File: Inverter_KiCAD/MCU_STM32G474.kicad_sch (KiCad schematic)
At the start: 42 parts, among them J801 USB_C_Receptacle_USB2.0, J802 Conn_01x05, J803 Conn_ST_STDC14, J804 Conn_01x04, SW801 SW_Push, SW802 SW_Push, SW803 SW_Push, SW804 SW_Push, SW805 SW_Push, U801 STM32G474RETx, U802 USBLC6-2SC6, Y801 16M

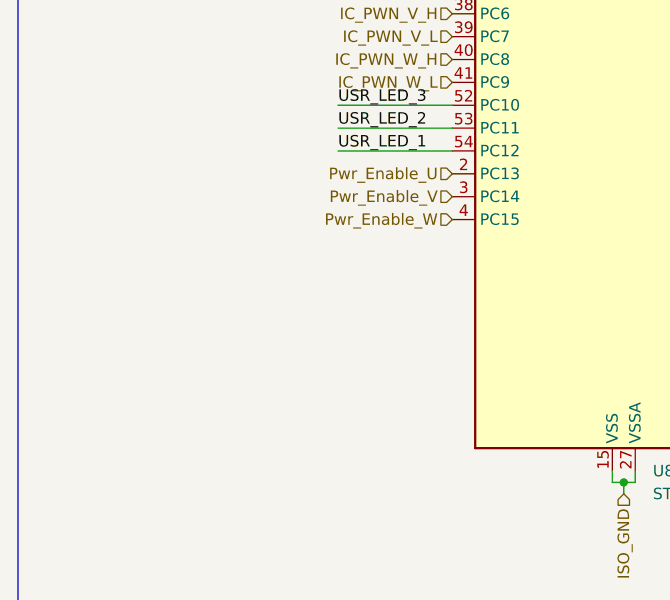
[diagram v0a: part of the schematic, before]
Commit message: add command sheet
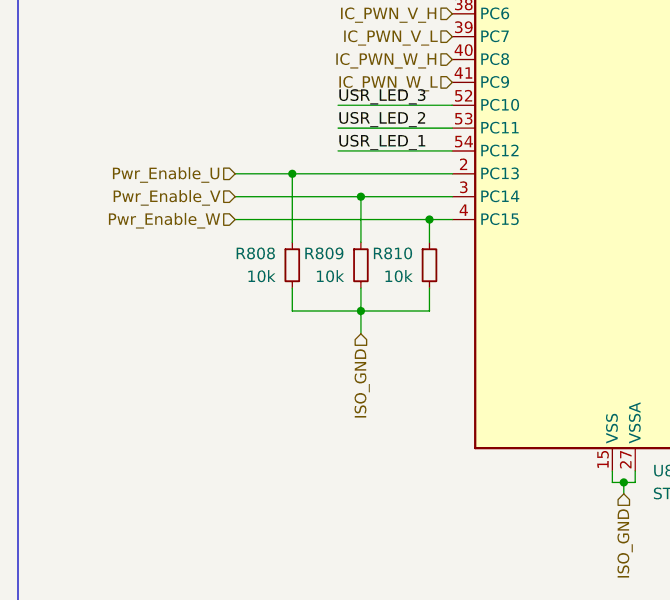
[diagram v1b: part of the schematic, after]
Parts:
- added R808, R809, R810: 10k, Resistor_SMD:R_0402_1005Metric, symbol Device:R_Small
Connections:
- net ISO_GND: now also R808.2, R809.2, R810.2
- net Pwr_Enable_U: now also R808.1
- net Pwr_Enable_V: now also R809.1
- net Pwr_Enable_W: now also R810.1
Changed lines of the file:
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@@
   (junction (at 29.21 57.15) (diameter 0) (color 0 0 0 0)
   )
+  (junction (at 52.07 116.84) (diameter 0) (color 0 0 0 0)
+  )
   (junction (at 213.36 148.59) (diameter 0) (color 0 0 0 0)
   )
@@
   (junction (at 166.37 46.99) (diameter 0) (color 0 0 0 0)
   )
+  (junction (at 59.69 106.68) (diameter 0) (color 0 0 0 0)
+  )
   (junction (at 278.13 33.02) (diameter 0) (color 0 0 0 0)
   )
@@
   (junction (at 194.31 40.64) (diameter 0) (color 0 0 0 0)
   )
+  (junction (at 52.07 104.14) (diameter 0) (color 0 0 0 0)
+  )
   (junction (at 175.26 54.61) (diameter 0) (color 0 0 0 0)
   )
@@
   )
   (junction (at 166.37 138.43) (diameter 0) (color 0 0 0 0)
+  )
+  (junction (at 44.45 101.6) (diameter 0) (color 0 0 0 0)
   )
   (junction (at 81.28 135.89) (diameter 0) (color 0 0 0 0)
@@
     (stroke (width 0) (type default))
   )
+  (wire (pts (xy 44.45 101.6) (xy 44.45 109.22))
+    (stroke (width 0) (type default))
+  )
   (wire (pts (xy 269.24 111.76) (xy 271.78 111.76))
     (stroke (width 0) (type default))
@@
     (stroke (width 0) (type default))
   )
+  (wire (pts (xy 52.07 116.84) (xy 59.69 116.84))
+    (stroke (width 0) (type default))
+  )
   (wire (pts (xy 74.93 40.64) (xy 74.93 39.37))
     (stroke (width 0) (type default))
@@
     (stroke (width 0) (type default))
   )
+  (wire (pts (xy 59.69 106.68) (xy 59.69 109.22))
+    (stroke (width 0) (type default))
+  )
   (wire (pts (xy 220.98 21.59) (xy 222.25 21.59))
     (stroke (width 0) (type default))
@@
     (stroke (width 0) (type default))
   )
+  (wire (pts (xy 59.69 106.68) (xy 62.23 106.68))
+    (stroke (width 0) (type default))
+  )
   (wire (pts (xy 176.53 99.06) (xy 180.34 99.06))
     (stroke (width 0) (type default))
@@
     (stroke (width 0) (type default))
   )
+  (wire (pts (xy 44.45 101.6) (xy 62.23 101.6))
+    (stroke (width 0) (type default))
+  )
   (wire (pts (xy 250.19 93.98) (xy 259.08 93.98))
     (stroke (width 0) (type default))
@@
     (stroke (width 0) (type default))
   )
+  (wire (pts (xy 38.1 104.14) (xy 52.07 104.14))
+    (stroke (width 0) (type default))
+  )
   (wire (pts (xy 269.24 135.89) (xy 269.24 128.27))
     (stroke (width 0) (type default))
@@
     (stroke (width 0) (type default))
   )
+  (wire (pts (xy 44.45 114.3) (xy 44.45 116.84))
+    (stroke (width 0) (type default))
+  )
+  (wire (pts (xy 52.07 104.14) (xy 62.23 104.14))
+    (stroke (width 0) (type default))
+  )
   (wire (pts (xy 82.55 134.62) (xy 82.55 135.89))
     (stroke (width 0) (type default))
@@
     (stroke (width 0) (type default))
   )
+  (wire (pts (xy 52.07 109.22) (xy 52.07 104.14))
+    (stroke (width 0) (type default))
+  )
+  (wire (pts (xy 38.1 101.6) (xy 44.45 101.6))
+    (stroke (width 0) (type default))
+  )
   (wire (pts (xy 267.97 24.13) (xy 270.51 24.13))
     (stroke (width 0) (type default))
@@
     (stroke (width 0) (type default))
   )
+  (wire (pts (xy 44.45 116.84) (xy 52.07 116.84))
+    (stroke (width 0) (type default))
+  )
   (wire (pts (xy 180.34 95.25) (xy 182.88 95.25))
     (stroke (width 0) (type default))
@@
     (stroke (width 0) (type default))
   )
+  (wire (pts (xy 52.07 114.3) (xy 52.07 116.84))
+    (stroke (width 0) (type default))
+  )
   (wire (pts (xy 30.48 52.07) (xy 29.21 52.07))
     (stroke (width 0) (type default))
@@
     (stroke (width 0) (type default))
   )
+  (wire (pts (xy 52.07 116.84) (xy 52.07 119.38))
+    (stroke (width 0) (type default))
+  )
+  (wire (pts (xy 38.1 106.68) (xy 59.69 106.68))
+    (stroke (width 0) (type default))
+  )
   (wire (pts (xy 223.52 63.5) (xy 220.98 63.5))
     (stroke (width 0) (type default))
@@
   )
   (wire (pts (xy 77.47 40.64) (xy 77.47 39.37))
+    (stroke (width 0) (type default))
+  )
+  (wire (pts (xy 59.69 114.3) (xy 59.69 116.84))
     (stroke (width 0) (type default))
   )
@@
     (effects (font (size 1.27 1.27)) (justify right))
   )
-  (hierarchical_label "Pwr_Enable_W" (shape input) (at 62.23 106.68 180) (fields_autoplaced)
-    (effects (font (size 1.27 1.27)) (justify right))
-  )
-  (hierarchical_label "Pwr_Enable_U" (shape input) (at 62.23 101.6 180) (fields_autoplaced)
+  (hierarchical_label "Pwr_Enable_W" (shape input) (at 38.1 106.68 180) (fields_autoplaced)
+    (effects (font (size 1.27 1.27)) (justify right))
+  )
+  (hierarchical_label "Pwr_Enable_U" (shape input) (at 38.1 101.6 180) (fields_autoplaced)
     (effects (font (size 1.27 1.27)) (justify right))
   )
@@
     (effects (font (size 1.27 1.27)) (justify right))
   )
+  (hierarchical_label "ISO_GND" (shape input) (at 52.07 119.38 270) (fields_autoplaced)
+    (effects (font (size 1.27 1.27)) (justify right))
+  )
   (hierarchical_label "W_Imes" (shape input) (at 97.79 121.92 0) (fields_autoplaced)
     (effects (font (size 1.27 1.27)) (justify left))
@@
     (effects (font (size 1.27 1.27)) (justify left))
   )
-  (hierarchical_label "Pwr_Enable_V" (shape input) (at 62.23 104.14 180) (fields_autoplaced)
+  (hierarchical_label "Pwr_Enable_V" (shape input) (at 38.1 104.14 180) (fields_autoplaced)
     (effects (font (size 1.27 1.27)) (justify right))
   )
@@
     )
   )
+  (symbol (lib_id "Device:R_Small") (at 59.69 111.76 0) (unit 1)
+    (in_bom yes) (on_board yes) (dnp no)
+    (property "Reference" "R810" (at 53.34 110.49 0)
+      (effects (font (size 1.27 1.27)) (justify left))
+    )
+    (property "Value" "10k" (at 54.61 113.03 0)
+      (effects (font (size 1.27 1.27)) (justify left))
+    )
+    (property "Footprint" "Resistor_SMD:R_0402_1005Metric" (at 59.69 111.76 0)
+      (effects (font (size 1.27 1.27)) hide)
+    )
+    (property "Datasheet" "~" (at 59.69 111.76 0)
+      (effects (font (size 1.27 1.27)) hide)
+    )
+    (property "Fournisseur" "Sotck" (at 59.69 111.76 0)
+      (effects (font (size 1.27 1.27)) hide)
+    )
+    (pin "1")
+    (pin "2")
+    (instances
+      (project "Inverter_KiCAD"
+        (path "/5e6c1e3f-0815-454a-8acb-8e3e2d064875/98f7f190-4cd6-4f5a-9ea2-2a00e81dec72"
+          (reference "R810") (unit 1)
+        )
+      )
+    )
+  )
   (symbol (lib_id "Device:R_Small") (at 273.05 41.91 90) (unit 1)
     (in_bom yes) (on_board yes) (dnp no) (fields_autoplaced)
@@
         (path "/5e6c1e3f-0815-454a-8acb-8e3e2d064875/98f7f190-4cd6-4f5a-9ea2-2a00e81dec72"
           (reference "C809") (unit 1)
+        )
+      )
+    )
+  )
+  (symbol (lib_id "Device:R_Small") (at 52.07 111.76 0) (unit 1)
+    (in_bom yes) (on_board yes) (dnp no)
+    (property "Reference" "R809" (at 45.72 110.49 0)
+      (effects (font (size 1.27 1.27)) (justify left))
+    )
+    (property "Value" "10k" (at 46.99 113.03 0)
+      (effects (font (size 1.27 1.27)) (justify left))
+    )
+    (property "Footprint" "Resistor_SMD:R_0402_1005Metric" (at 52.07 111.76 0)
+      (effects (font (size 1.27 1.27)) hide)
+    )
+    (property "Datasheet" "~" (at 52.07 111.76 0)
+      (effects (font (size 1.27 1.27)) hide)
+    )
+    (property "Fournisseur" "Sotck" (at 52.07 111.76 0)
+      (effects (font (size 1.27 1.27)) hide)
+    )
+    (pin "1")
+    (pin "2")
+    (instances
+      (project "Inverter_KiCAD"
+        (path "/5e6c1e3f-0815-454a-8acb-8e3e2d064875/98f7f190-4cd6-4f5a-9ea2-2a00e81dec72"
+          (reference "R809") (unit 1)
         )
       )
@@
         )
       )
+    )
+  )
+  (symbol (lib_id "Device:R_Small") (at 44.45 111.76 0) (unit 1)
+    (in_bom yes) (on_board yes) (dnp no)
+    (property "Reference" "R808" (at 38.1 110.49 0)
+      (effects (font (size 1.27 1.27)) (justify left))
+    )
+    (property "Value" "10k" (at 39.37 113.03 0)
+      (effects (font (size 1.27 1.27)) (justify left))
+    )
+    (property "Footprint" "Resistor_SMD:R_0402_1005Metric" (at 44.45 111.76 0)
+      (effects (font (size 1.27 1.27)) hide)
+    )
+    (property "Datasheet" "~" (at 44.45 111.76 0)
+      (effects (font (size 1.27 1.27)) hide)
+    )
+    (property "Fournisseur" "Sotck" (at 44.45 111.76 0)
+      (effects (font (size 1.27 1.27)) hide)
+    )
+    (pin "1")
+    (pin "2")
+    (instances
+      (project "Inverter_KiCAD"
+        (path "/5e6c1e3f-0815-454a-8acb-8e3e2d064875/98f7f190-4cd6-4f5a-9ea2-2a00e81dec72"
+          (reference "R808") (unit 1)
+        )
+      )

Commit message: update pcb
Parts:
- renumbered R808 to R801, R809 to R802, R810 to R803, R801 to R804, R802 to R805, R803 to R806, R804 to R807, R805 to R808, R806 to R809, R807 to R810
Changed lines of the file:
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@@
   (symbol (lib_id "Device:R_Small") (at 273.05 33.02 90) (unit 1)
     (in_bom yes) (on_board yes) (dnp no) (fields_autoplaced)
-    (property "Reference" "R805" (at 273.05 27.94 90)
+    (property "Reference" "R808" (at 273.05 27.94 90)
       (effects (font (size 1.27 1.27)))
     )
@@
       (project "Inverter_KiCAD"
         (path "/5e6c1e3f-0815-454a-8acb-8e3e2d064875/98f7f190-4cd6-4f5a-9ea2-2a00e81dec72"
-          (reference "R805") (unit 1)
+          (reference "R808") (unit 1)
         )
       )
@@
   (symbol (lib_id "Device:R_Small") (at 189.23 91.44 90) (unit 1)
     (in_bom yes) (on_board yes) (dnp no) (fields_autoplaced)
-    (property "Reference" "R803" (at 188.595 88.9 0)
+    (property "Reference" "R806" (at 188.595 88.9 0)
       (effects (font (size 1.27 1.27)) (justify left))
     )
@@
       (project "Inverter_KiCAD"
         (path "/5e6c1e3f-0815-454a-8acb-8e3e2d064875/98f7f190-4cd6-4f5a-9ea2-2a00e81dec72"
-          (reference "R803") (unit 1)
+          (reference "R806") (unit 1)
         )
       )
@@
   (symbol (lib_id "Device:R_Small") (at 113.03 109.22 90) (unit 1)
     (in_bom yes) (on_board yes) (dnp no)
-    (property "Reference" "R801" (at 116.84 106.68 90)
+    (property "Reference" "R804" (at 116.84 106.68 90)
       (effects (font (size 1.27 1.27)))
     )
@@
       (project "Inverter_KiCAD"
         (path "/5e6c1e3f-0815-454a-8acb-8e3e2d064875/98f7f190-4cd6-4f5a-9ea2-2a00e81dec72"
-          (reference "R801") (unit 1)
+          (reference "R804") (unit 1)
         )
       )
@@
   (symbol (lib_id "Device:R_Small") (at 59.69 111.76 0) (unit 1)
     (in_bom yes) (on_board yes) (dnp no)
-    (property "Reference" "R810" (at 53.34 110.49 0)
+    (property "Reference" "R803" (at 53.34 110.49 0)
       (effects (font (size 1.27 1.27)) (justify left))
     )
@@
       (project "Inverter_KiCAD"
         (path "/5e6c1e3f-0815-454a-8acb-8e3e2d064875/98f7f190-4cd6-4f5a-9ea2-2a00e81dec72"
-          (reference "R810") (unit 1)
+          (reference "R803") (unit 1)
         )
       )
@@
   (symbol (lib_id "Device:R_Small") (at 273.05 41.91 90) (unit 1)
     (in_bom yes) (on_board yes) (dnp no) (fields_autoplaced)
-    (property "Reference" "R806" (at 273.05 36.83 90)
+    (property "Reference" "R809" (at 273.05 36.83 90)
       (effects (font (size 1.27 1.27)))
     )
@@
       (project "Inverter_KiCAD"
         (path "/5e6c1e3f-0815-454a-8acb-8e3e2d064875/98f7f190-4cd6-4f5a-9ea2-2a00e81dec72"
-          (reference "R806") (unit 1)
+          (reference "R809") (unit 1)
         )
       )
@@
   (symbol (lib_id "Device:R_Small") (at 189.23 83.82 90) (unit 1)
     (in_bom yes) (on_board yes) (dnp no) (fields_autoplaced)
-    (property "Reference" "R802" (at 188.595 81.28 0)
+    (property "Reference" "R805" (at 188.595 81.28 0)
       (effects (font (size 1.27 1.27)) (justify left))
     )
@@
       (project "Inverter_KiCAD"
         (path "/5e6c1e3f-0815-454a-8acb-8e3e2d064875/98f7f190-4cd6-4f5a-9ea2-2a00e81dec72"
-          (reference "R802") (unit 1)
+          (reference "R805") (unit 1)
         )
       )
@@
   (symbol (lib_id "Device:R_Small") (at 52.07 111.76 0) (unit 1)
     (in_bom yes) (on_board yes) (dnp no)
-    (property "Reference" "R809" (at 45.72 110.49 0)
+    (property "Reference" "R802" (at 45.72 110.49 0)
       (effects (font (size 1.27 1.27)) (justify left))
     )
@@
       (project "Inverter_KiCAD"
         (path "/5e6c1e3f-0815-454a-8acb-8e3e2d064875/98f7f190-4cd6-4f5a-9ea2-2a00e81dec72"
-          (reference "R809") (unit 1)
+          (reference "R802") (unit 1)
         )
       )
@@
   (symbol (lib_id "Device:R_Small") (at 273.05 50.8 90) (unit 1)
     (in_bom yes) (on_board yes) (dnp no) (fields_autoplaced)
-    (property "Reference" "R807" (at 273.05 45.72 90)
+    (property "Reference" "R810" (at 273.05 45.72 90)
       (effects (font (size 1.27 1.27)))
     )
@@
       (project "Inverter_KiCAD"
         (path "/5e6c1e3f-0815-454a-8acb-8e3e2d064875/98f7f190-4cd6-4f5a-9ea2-2a00e81dec72"
-          (reference "R807") (unit 1)
+          (reference "R810") (unit 1)
         )
       )
@@
   (symbol (lib_id "Device:R_Small") (at 44.45 111.76 0) (unit 1)
     (in_bom yes) (on_board yes) (dnp no)
-    (property "Reference" "R808" (at 38.1 110.49 0)
+    (property "Reference" "R801" (at 38.1 110.49 0)
       (effects (font (size 1.27 1.27)) (justify left))
     )
@@
       (project "Inverter_KiCAD"
         (path "/5e6c1e3f-0815-454a-8acb-8e3e2d064875/98f7f190-4cd6-4f5a-9ea2-2a00e81dec72"
-          (reference "R808") (unit 1)
+          (reference "R801") (unit 1)
         )
       )
@@
   (symbol (lib_id "Device:R_Small") (at 273.05 24.13 90) (unit 1)
     (in_bom yes) (on_board yes) (dnp no) (fields_autoplaced)
-    (property "Reference" "R804" (at 273.05 19.05 90)
+    (property "Reference" "R807" (at 273.05 19.05 90)
       (effects (font (size 1.27 1.27)))
     )
@@
       (project "Inverter_KiCAD"
         (path "/5e6c1e3f-0815-454a-8acb-8e3e2d064875/98f7f190-4cd6-4f5a-9ea2-2a00e81dec72"
-          (reference "R804") (unit 1)
-        )
-      )
+          (reference "R807") (unit 1)
+        )
+      )
